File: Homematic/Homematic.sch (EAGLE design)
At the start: 30 parts, among them IC1 3.3V, IC2 3.3V, P1 DF11-06-2DS, Q1 BC337-40

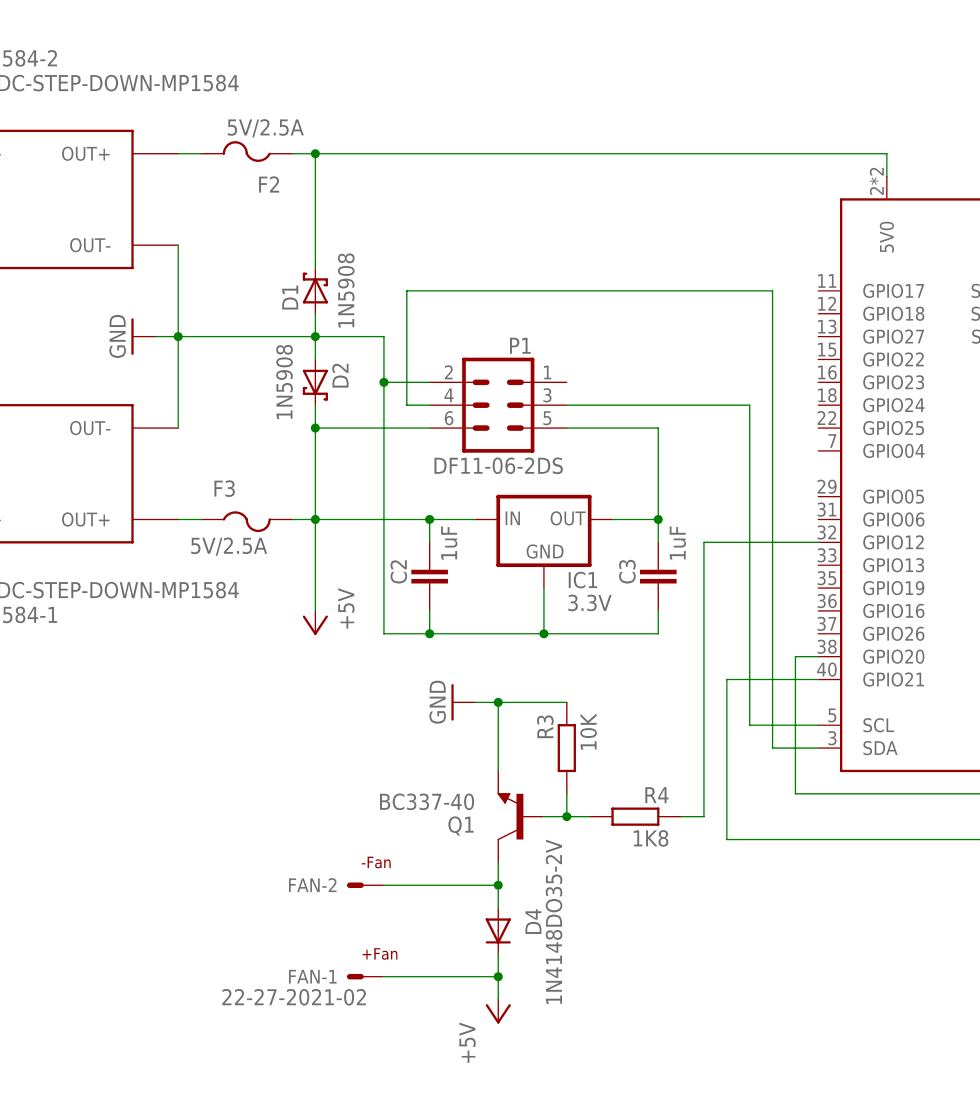
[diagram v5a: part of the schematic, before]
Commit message: Increase drill for mount holes. Add antenna connector legend. Fine tune ground plate contour.
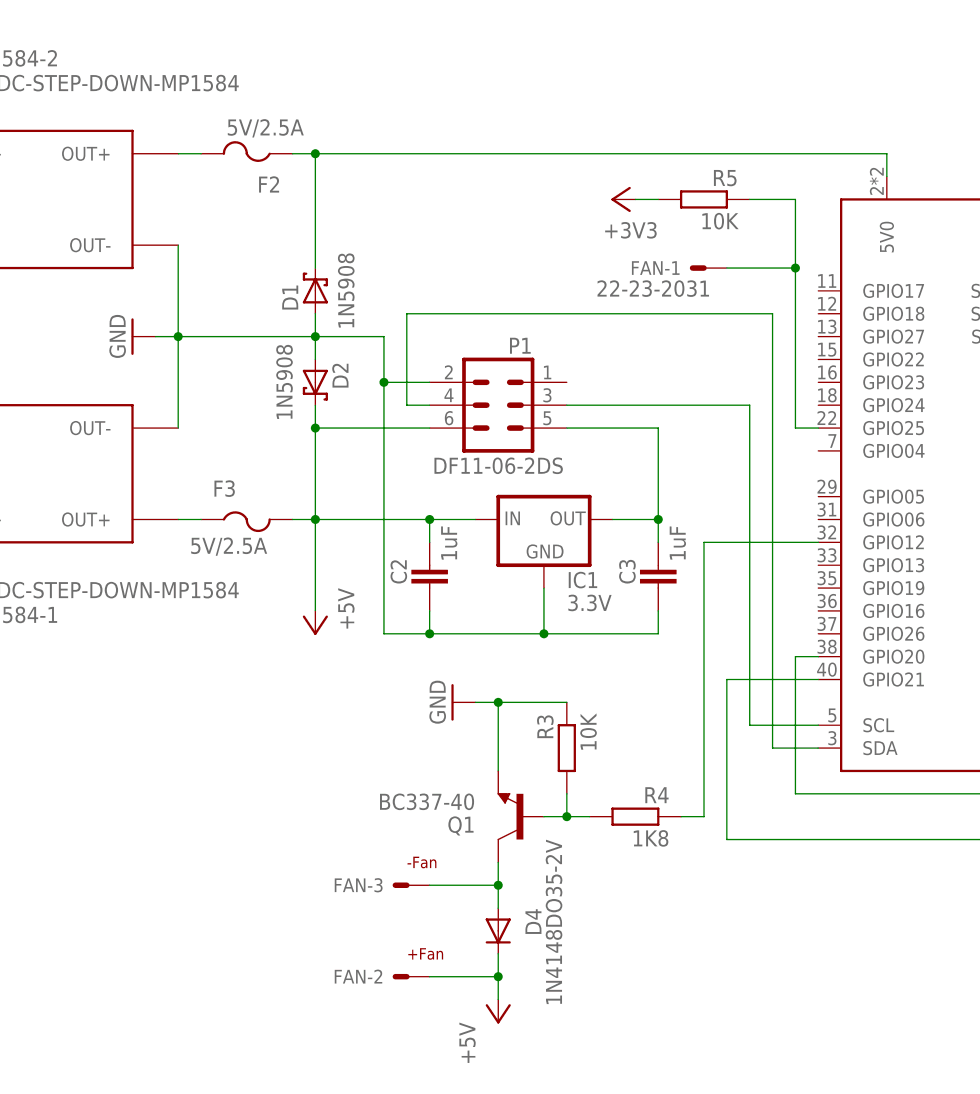
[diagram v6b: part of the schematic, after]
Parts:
- added R5: 10K, rcl:R-EU_0204/2V
- FAN: value 22-27-2021-02 -> 22-23-2031; device con-molex:22-27-2021-02 -> con-molex:22-23-2031
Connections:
- new net N$22: FAN-1.S, R5.1, RPI.GPIO25
- net +3V3: now also R5.2
- net +5V: now also FAN-2.S; no longer FAN-1.S
- net N$14: now also FAN-3.S; no longer FAN-2.S
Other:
- moved on the sheet: FAN-1, FAN-2
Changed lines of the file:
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@@
 <part name="P+4" library="supply1" deviceset="+5V" device=""/>
 <part name="GND8" library="supply1" deviceset="GND" device=""/>
-<part name="FAN" library="con-molex" deviceset="22-?-02" device="27-2021"/>
+<part name="FAN" library="con-molex" deviceset="22-23-2031" device=""/>
+<part name="R5" library="rcl" deviceset="R-EU_" device="0204/2V" value="10K">
+<attribute name="MF" value=""/>
+<attribute name="MPN" value=""/>
+<attribute name="OC_FARNELL" value="unknown"/>
+</part>
+<part name="+3V3" library="supply1" deviceset="+3V3" device=""/>
 </parts>
 <sheets>
@@
 <text x="5.08" y="81.28" size="1.27" layer="94" font="vector" ratio="10" rot="MR180" align="center-left">+24V</text>
 <text x="5.08" y="78.74" size="1.27" layer="94" font="vector" ratio="10" rot="MR180" align="center-left">-24V</text>
-<text x="93.98" y="20.32" size="1.27" layer="94" font="vector" ratio="10" rot="MR180" align="center-left">-Fan</text>
-<text x="93.98" y="10.16" size="1.27" layer="94" font="vector" ratio="10" rot="MR180" align="center-left">+Fan</text>
+<text x="99.06" y="20.32" size="1.27" layer="94" font="vector" ratio="10" rot="MR180" align="center-left">-Fan</text>
+<text x="99.06" y="10.16" size="1.27" layer="94" font="vector" ratio="10" rot="MR180" align="center-left">+Fan</text>
 </plain>
 <instances>
@@
 </instance>
 <instance part="GND8" gate="1" x="104.14" y="38.1" rot="R270"/>
-<instance part="FAN" gate="-1" x="93.98" y="7.62" rot="R180"/>
-<instance part="FAN" gate="-2" x="93.98" y="17.78" rot="R180"/>
+<instance part="FAN" gate="-1" x="132.08" y="86.36" rot="R180"/>
+<instance part="FAN" gate="-2" x="99.06" y="7.62" rot="R180"/>
+<instance part="FAN" gate="-3" x="99.06" y="17.78" rot="R180"/>
+<instance part="R5" gate="G$1" x="132.08" y="93.98" rot="MR0">
+<attribute name="OC_FARNELL" x="132.08" y="93.98" size="1.778" layer="96" rot="MR270" display="off"/>
+<attribute name="MF" x="132.08" y="93.98" size="1.778" layer="96" rot="MR270" display="off"/>
+<attribute name="MPN" x="132.08" y="93.98" size="1.778" layer="96" rot="MR270" display="off"/>
+</instance>
+<instance part="+3V3" gate="G$1" x="121.92" y="93.98" rot="R90"/>
 </instances>
 <busses>
@@
 <pinref part="P1" gate="G$1" pin="4"/>
 <wire x1="101.6" y1="71.12" x2="99.06" y2="71.12" width="0.1524" layer="91"/>
-<wire x1="99.06" y1="71.12" x2="99.06" y2="83.82" width="0.1524" layer="91"/>
-<wire x1="99.06" y1="83.82" x2="139.7" y2="83.82" width="0.1524" layer="91"/>
-<wire x1="139.7" y1="83.82" x2="139.7" y2="33.02" width="0.1524" layer="91"/>
+<wire x1="99.06" y1="71.12" x2="99.06" y2="81.28" width="0.1524" layer="91"/>
+<wire x1="99.06" y1="81.28" x2="139.7" y2="81.28" width="0.1524" layer="91"/>
+<wire x1="139.7" y1="81.28" x2="139.7" y2="33.02" width="0.1524" layer="91"/>
 <pinref part="RPI" gate="G$1" pin="SDA"/>
 <wire x1="139.7" y1="33.02" x2="144.78" y2="33.02" width="0.1524" layer="91"/>
@@
 <wire x1="109.22" y1="7.62" x2="109.22" y2="5.08" width="0.1524" layer="91"/>
 <junction x="109.22" y="7.62"/>
-<pinref part="FAN" gate="-1" pin="S"/>
-<wire x1="96.52" y1="7.62" x2="109.22" y2="7.62" width="0.1524" layer="91"/>
+<pinref part="FAN" gate="-2" pin="S"/>
+<wire x1="101.6" y1="7.62" x2="109.22" y2="7.62" width="0.1524" layer="91"/>
 </segment>
 </net>
@@
 <junction x="213.36" y="45.72"/>
 </segment>
+<segment>
+<pinref part="+3V3" gate="G$1" pin="+3V3"/>
+<pinref part="R5" gate="G$1" pin="2"/>
+<wire x1="124.46" y1="93.98" x2="127" y2="93.98" width="0.1524" layer="91"/>
+</segment>
 </net>
 <net name="N$2" class="0">
@@
 <pinref part="Q1" gate="G$1" pin="C"/>
 <wire x1="109.22" y1="15.24" x2="109.22" y2="17.78" width="0.1524" layer="91"/>
+<pinref part="FAN" gate="-3" pin="S"/>
 <wire x1="109.22" y1="17.78" x2="109.22" y2="20.32" width="0.1524" layer="91"/>
+<wire x1="101.6" y1="17.78" x2="109.22" y2="17.78" width="0.1524" layer="91"/>
 <junction x="109.22" y="17.78"/>
-<pinref part="FAN" gate="-2" pin="S"/>
-<wire x1="96.52" y1="17.78" x2="109.22" y2="17.78" width="0.1524" layer="91"/>
 </segment>
 </net>
@@
 </segment>
 </net>
+<net name="N$22" class="0">
+<segment>
+<pinref part="RPI" gate="G$1" pin="GPIO25"/>
+<wire x1="144.78" y1="68.58" x2="142.24" y2="68.58" width="0.1524" layer="91"/>
+<wire x1="142.24" y1="68.58" x2="142.24" y2="86.36" width="0.1524" layer="91"/>
+<pinref part="R5" gate="G$1" pin="1"/>
+<pinref part="FAN" gate="-1" pin="S"/>
+<wire x1="142.24" y1="86.36" x2="142.24" y2="93.98" width="0.1524" layer="91"/>
+<wire x1="142.24" y1="93.98" x2="137.16" y2="93.98" width="0.1524" layer="91"/>
+<wire x1="134.62" y1="86.36" x2="142.24" y2="86.36" width="0.1524" layer="91"/>
+<junction x="142.24" y="86.36"/>
+</segment>
+</net>

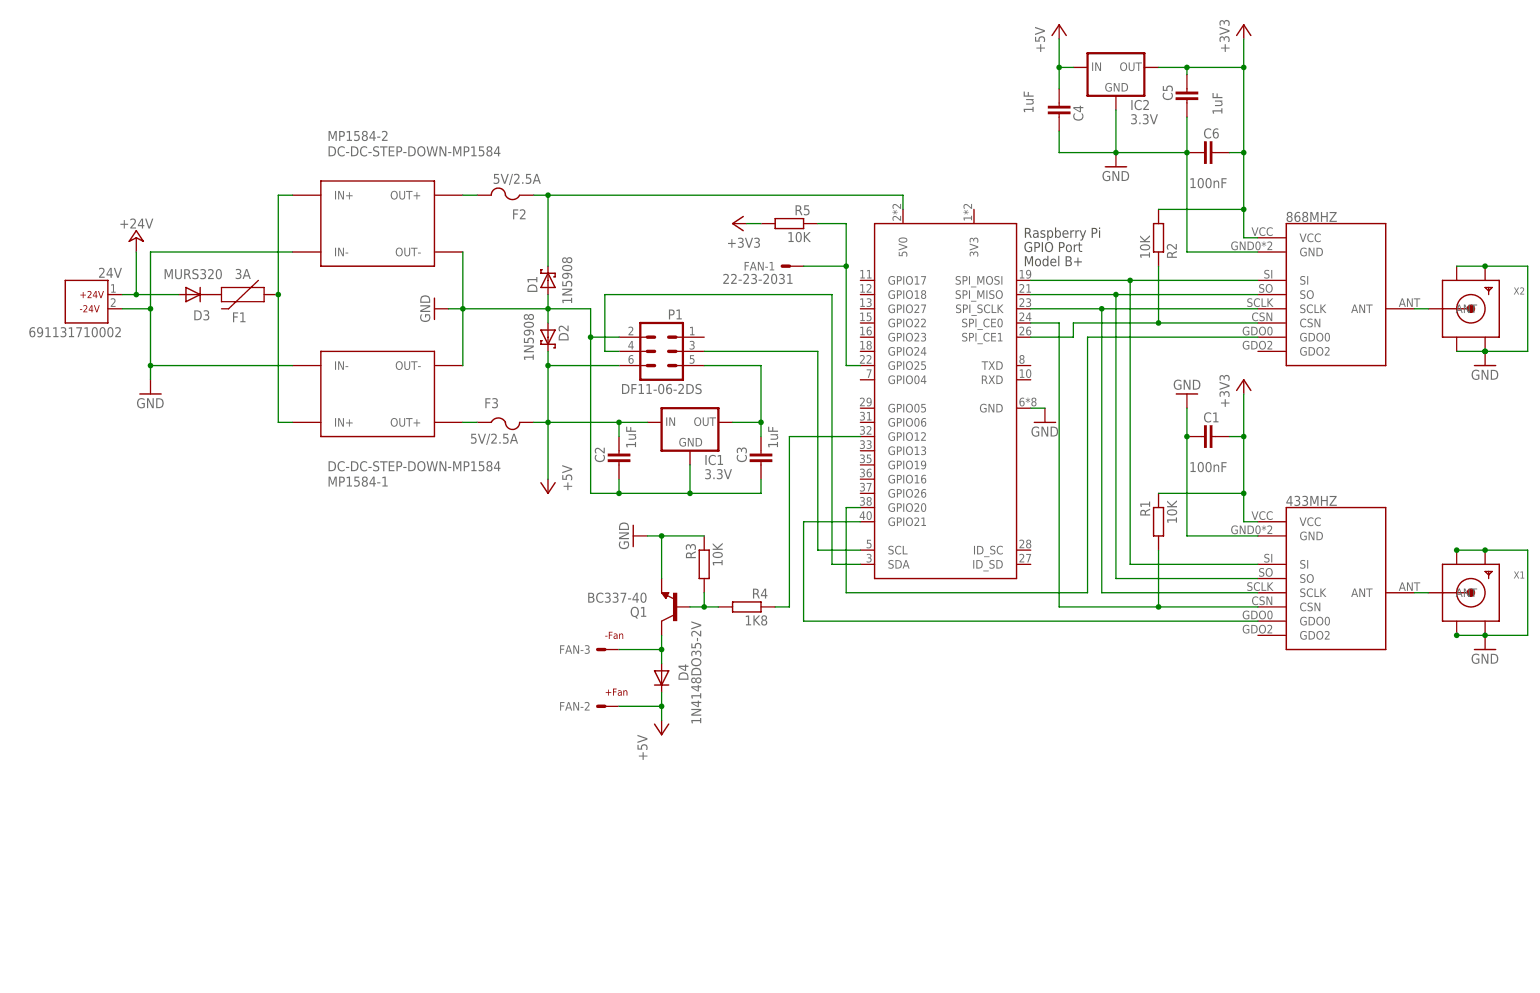
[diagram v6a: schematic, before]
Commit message: Add power switch and I2C interrupt wire. Add pull-up resistors for I2C. Adapt drills.
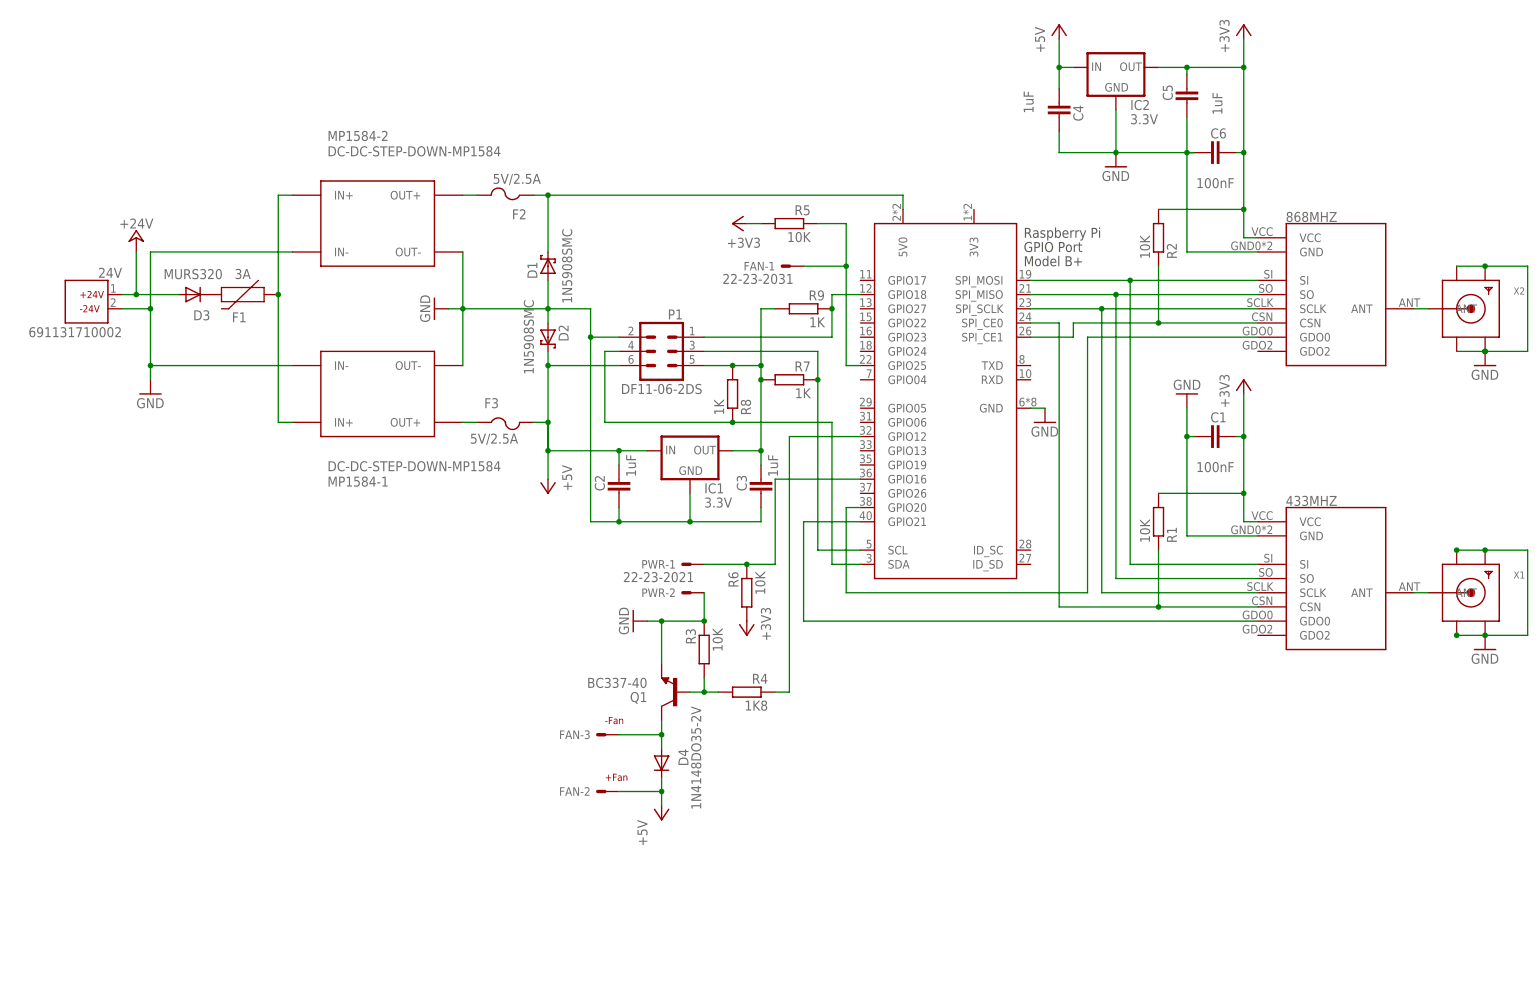
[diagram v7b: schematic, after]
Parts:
- added PWR: 22-23-2021, con-molex:22-23-2021
- added R6: 10K, rcl:R-EU_0204/2V
- added R7, R8, R9: 1K, rcl:R-EU_0204/2V
- D1, D2: value 1N5908 -> 1N5908SMC; device diode:1N5908 -> diode:1N5908SMC
- IC1, IC2: device adafruit:MCP1700TRI -> mcp:MCP1700TRI
- R1: device rcl:R-EU_0204/5 -> rcl:R-EU_0204/2V
- RPI: value RASPI_BOARD_B+#_F -> RASPI_BOARD_B+#_4F; device raspberrypi_bastelstube_v13:RASPI_BOARD_B+#_F -> raspberrypi_bastelstube_v13:RASPI_BOARD_B+#_4F
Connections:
- new net N$21: PWR-1.S, R6.1, RPI.GPIO16
- new net N$23: P1.1, R9.1, RPI.GPIO18
- net +3V3: now also R1.2, R6.2; no longer R1.1
- net GND: now also PWR-2.S
- net N$1: now also R7.1
- net N$12: now also R8.1
- net N$2: now also R7.2, R8.2, R9.2
- net N$3: now also R1.1; no longer R1.2
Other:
- moved on the sheet: C1, C2, C3, C6, D1, D4, FAN-2, FAN-3, IC1, Q1, R1, R3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

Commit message: Adapt for Raspberry Pi 4. I2C operate with 5V only. Add INT and RESET signals.
Signed-off-by: Alexander Falkenstern <alexander.falkenstern@gmail.com>
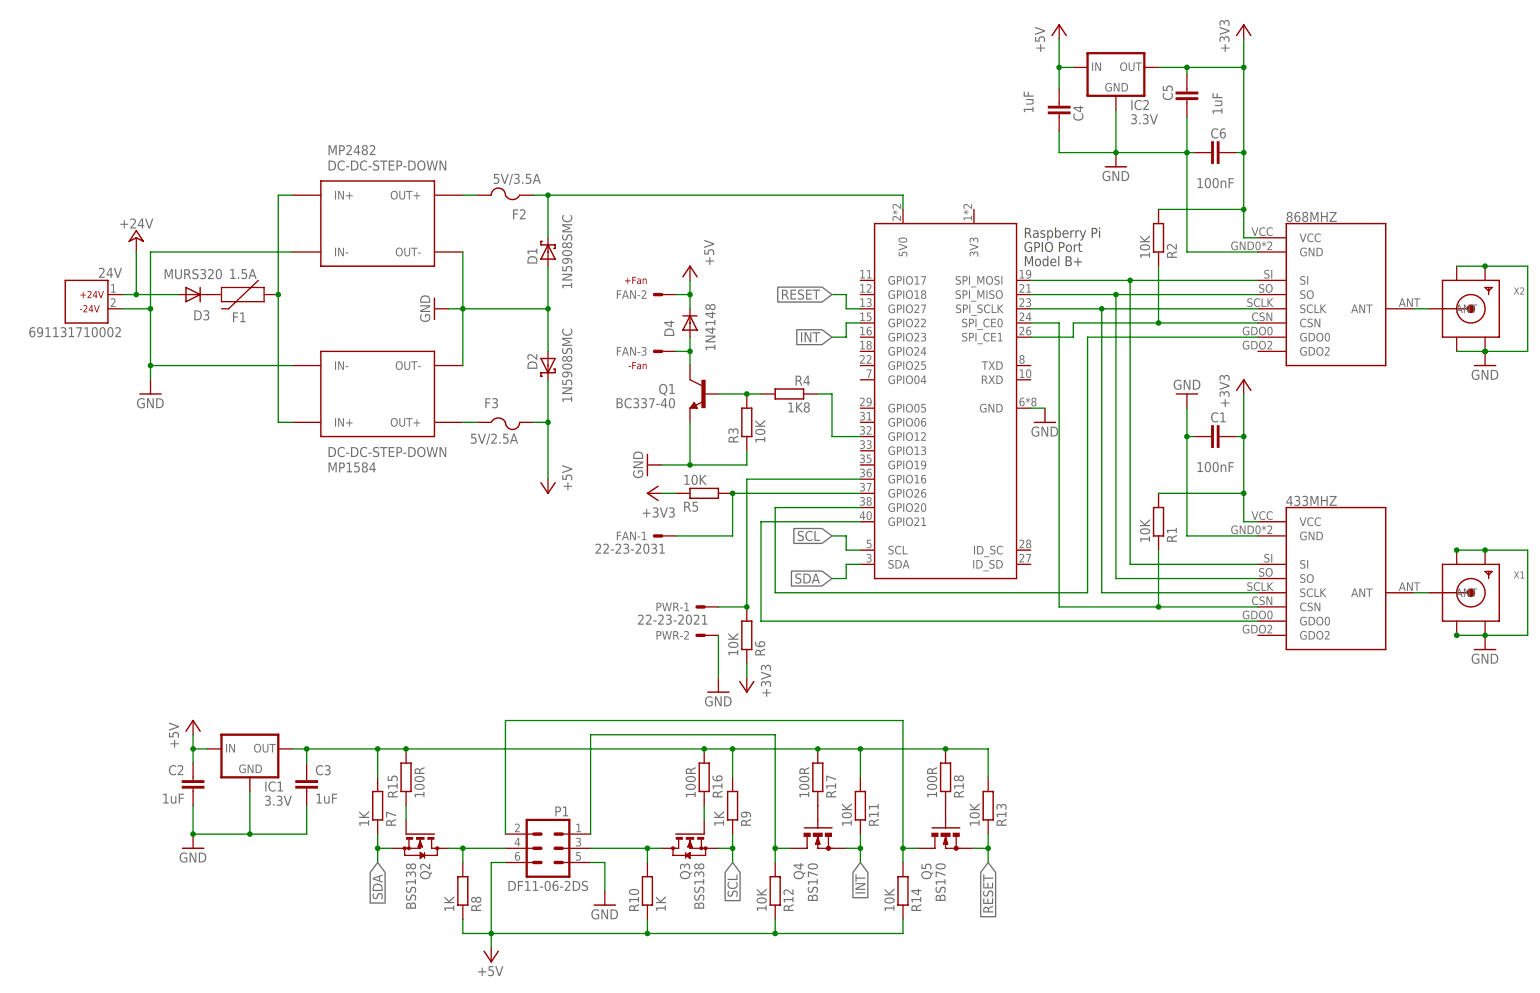
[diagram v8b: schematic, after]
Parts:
- removed MP1584-1, MP1584-2: DC-DC-STEP-DOWN-MP1584, modules:DC-DC-STEP-DOWN-MP1584
- added MP1584: DC-DC-STEP-DOWN, modules:DC-DC-STEP-DOWNMP1584
- added MP2482: DC-DC-STEP-DOWN, modules:DC-DC-STEP-DOWNMP2482
- added Q2, Q3: BSS138, transistor-small-signal:BSS123
- added Q4, Q5: BS170, transistor-small-signal:BS170
- added R10: 1K, rcl:R-EU_0204/2V
- added R11, R12, R13, R14: 10K, rcl:R-EU_0204/2V
- added R15, R16, R17, R18: 100R, rcl:R-EU_0204/2V
- D4: value 1N4148DO35-2V -> 1N4148
- F1: value 3A -> 1.5A
- F2: value 5V/2.5A -> 5V/3.5A
- RPI: device raspberrypi_bastelstube_v13:RASPI_BOARD_B+#_4F -> raspberrypi:RASPI_BOARD_B+#_4F
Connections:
- net N$5 renamed 5V0
- new net INT: Q4.S, R11.1, RPI.GPIO22
- new net N$24: Q3.G, R16.1
- new net N$25: P1.1, Q4.D, R12.2
- new net N$26: P1.2, Q5.D, R14.2
- new net N$27: Q5.G, R18.1
- new net N$28: Q4.G, R17.1
- new net RESET: Q5.S, R13.1, RPI.GPIO27
- new net SCL: Q3.S, R9.1, RPI.SCL
- new net SDA: Q2.S, R7.1, RPI.SDA
- net +3V3: now also R5.1, R6.1; no longer R5.2, R6.2
- net +5V: now also R10.1, R12.1, R14.1, R8.1
- net GND: now also MP1584.IN-, MP1584.OUT-, MP2482.IN-, MP2482.OUT-, P1.5; no longer MP1584-1.IN-, MP1584-1.OUT-, MP1584-2.IN-, MP1584-2.OUT-, P1.2
- net N$1: now also Q3.D, R10.2; no longer R7.1, RPI.SCL
- net N$12: now also Q2.D, R8.2; no longer R8.1, RPI.SDA
- net N$2: now also R11.2, R13.2, R15.2, R16.2, R17.2, R18.2; no longer P1.5, R8.2
- net N$21: now also R6.2; no longer R6.1
- net N$22: now also R5.2, RPI.GPIO26; no longer R5.1, RPI.GPIO25
- net N$23: now also Q2.G, R15.1; no longer P1.1, R9.1, RPI.GPIO18
- net N$4: now also MP2482.OUT+; no longer MP1584-2.OUT+
- net N$6: now also MP1584.OUT+; no longer MP1584-1.OUT+
- net N$7: now also MP1584.IN+, MP2482.IN+; no longer MP1584-1.IN+, MP1584-2.IN+
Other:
- moved on the sheet: C2, C3, D1, D2, D4, FAN-1, FAN-2, FAN-3, IC1, P1, PWR-1, PWR-2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
